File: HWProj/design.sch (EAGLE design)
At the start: 30 parts, among them IC1 LM311N, IC10 TL071P, IC11 TL071P, IC12 TL071P, IC2 TL071P, IC3 TL071P, IC4 TL071P, IC5 LM311N, IC6 TL071P, Q1 2N3904, Q2 2N3904

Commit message: begin designing entire schematic, added power
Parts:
- removed S1: TL32PO, switch:TL32PO
- added C2: 0.0022u, HyTechDevices:CAPCAP_WIMA
- added CN1: (no value), HyTechDevices:DCBARRELPTH
- added DC/DC1: DC/DC-STEP-UP-XL6009, userlib:DC/DC-STEP-UP-XL6009
- added IC13, IC14, IC15, IC17, IC7, IC8, IC9: TL071P, linear:TL071P
- added IC16: LM311N, linear:LM311N
- added Q3, Q4: 2N3904, transistor:2N3904
- added R10: 1.5M, HyTechDevices:RESISTORAXIAL-0.3
- added R12: 1.5k, HyTechDevices:RESISTORAXIAL-0.3
- added R13: 20k, HyTechDevices:RESISTORAXIAL-0.3
- added R14, R17, R18: 12k, HyTechDevices:RESISTORAXIAL-0.3
- added R15, R19, R20, R4: 10k, HyTechDevices:RESISTORAXIAL-0.3
- added R16, R21: 33k, HyTechDevices:RESISTORAXIAL-0.3
- added R9: 5.6k, HyTechDevices:RESISTORAXIAL-0.3
- added TM4: 50k, HyTechDevices:TRIMPOT
- added U$2: PAM8302A_ADAFRUIT, HyTechDevices:PAM8302A_ADAFRUIT
- added U$3: FQP30N06L, HyTechDevices:FQP30N06L
- added U$4: TEENSY_3.5_EXT, HyTechDevices:TEENSY_3.5_EXT
- C3, C4: device HyTechDevices:CAPCAP_WIMA -> HyTechDevices:CAPPTH1
- IC5: value LM311N -> TL071P; device linear:LM311N -> linear:TL071P
- IC6: value TL071P -> LM311N; device linear:TL071P -> linear:LM311N
- R1: value 20k -> 15k
- TM1: value 10K -> 50k
- TM2: value 10k -> 100k
- TM3: value 10k -> 10K
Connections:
- removed net VCO_FREQ_CONTROL: TM3.E
- new net +9V: CN1.PWR, DC/DC1.+VIN, U$4.VIN
- new net 11.5V: IC9.+IN, R4.1, R9.2
- new net COMP_SQ_OUT: IC16.OUT, IC8.+IN, R17.1, R20.2
- new net DGND: CN1.GND, CN1.GNDBREAK, DC/DC1.-VIN, U$4.AGND, U$4.GND
- new net N$13: IC7.OUT, R12.1
- new net N$15: IC6.ON, IC6.ON/STR
- new net N$16: IC15.-IN, IC15.OUT, U$3.G
- new net N$17: IC16.ON, IC16.ON/STR
- new net N$19: IC13.OUT, TM2.E, U$2.A+
- new net N$21: IC7.-IN, Q3.C, R10.1
- new net N$23: IC6.-IN, R18.1, R19.2
- new net N$24: IC1.-IN, R14.1, R15.2
- new net N$26: IC16.-IN, TM3.S
- new net N$28: IC5.-IN, R1.2, TM1.A, TM4.A
- new net N$3: Q3.E, Q4.E, R12.2
- new net SAWTOOTH2: C2.2, IC14.OUT, IC16.+IN, IC6.+IN, U$3.D
- new net SIGNAL1: Q1.B
- new net SIGNAL2: Q3.B
- new net VCC_LM386: IC9.-IN, IC9.OUT, U$2.VIN
- net GND: now also IC13.+IN, IC14.+IN, IC16.GND, IC16.V-, IC17.-IN, IC17.OUT, IC5.+IN, IC6.GND, IC7.+IN, Q4.B, R15.1, R19.1, R20.1, R9.1, U$2.A-, U$2.GND; no longer IC5.GND, TM1.A, TM2.A
- net INPUT2: now also IC5.OUT, R1.1; no longer S1.P
- net LOWPASS_OUT: now also TM2.A
- net N$1: now also IC17.+IN, R16.1, R21.2; no longer IC1.-IN, TM1.S
- net N$11: now also IC8.-IN, IC8.OUT; no longer IC5.ON, IC5.ON/STR
- net N$14: now also C2.1, IC14.-IN, Q4.C, U$3.S; no longer IC6.-IN, IC6.OUT, Q1.B
- net N$4: now also IC13.-IN, TM2.S; no longer IC6.+IN, TM3.S
- net N$8: now also IC15.+IN, IC6.OUT, R13.1; no longer IC5.-IN, TM2.S
- net SAWTOOTH: now also TM1.S; no longer IC5.+IN, S1.O
- net SQUARE: now also IC8.ON2, TM4.S; no longer IC5.OUT, R1.1, S1.S
- net V+: now also DC/DC1.+VOUT, IC13.V+, IC14.V+, IC15.V+, IC16.V+, IC17.V+, IC7.V+, IC8.V+, IC9.V+, R10.2, R13.2, R14.2, R16.2, R17.2, R18.2, R4.2, TM3.E; no longer R1.2, TM1.E, TM2.E
- net V-: now also DC/DC1.-VOUT, IC13.V-, IC14.V-, IC15.V-, IC17.V-, IC7.V-, IC8.V-, IC9.V-, R21.1
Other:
- note added: "+/-15V"
- note added: "add diff amp for signal isolation!!"
- note added: "digital"
- note added: "max 1Vrms input"
- note added: "mixing stage"
- note added: "power"
- note added: "speaker output stage"
- note added: "threshold at 6.8V!"
- note added: "volume control"
- note removed: "signal routing"
- note removed: "solution to create +/- 15V required"
- note removed: "threshold control"
- moved on the sheet: C3, C4, IC10, IC11, IC12, IC5, IC6, R1, R11, R5, R7, R8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

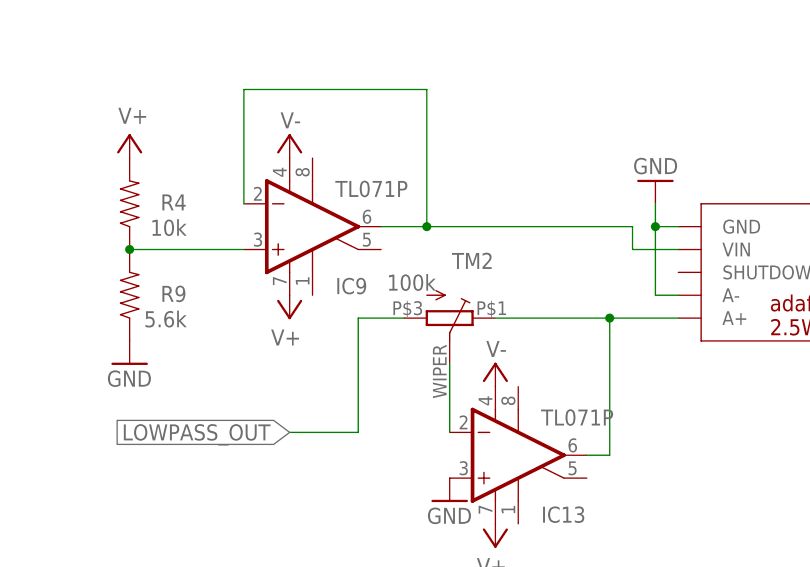
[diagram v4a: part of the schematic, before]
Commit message: changed value of volume control pot at speaker stage to 50k
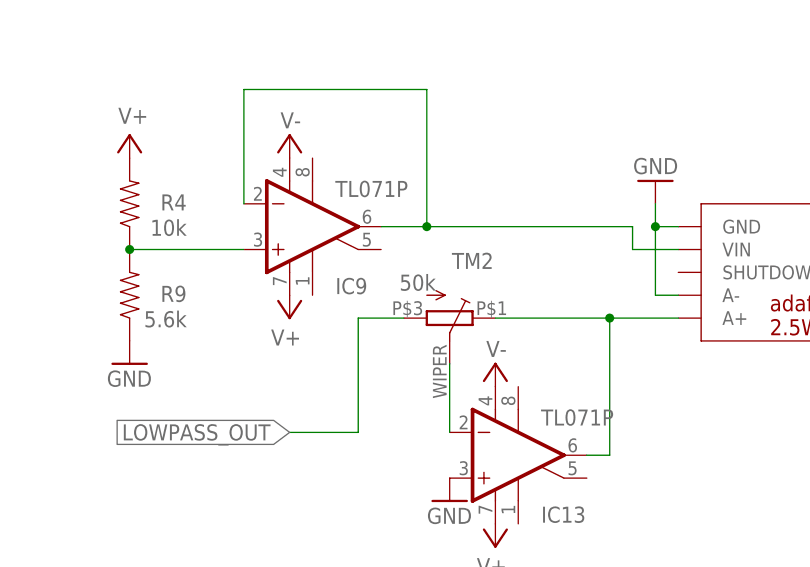
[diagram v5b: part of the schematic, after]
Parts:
- TM2: value 100k -> 50k
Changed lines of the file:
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@@
 <part name="IC13" library="linear" library_urn="urn:adsk.eagle:library:262" deviceset="TL071" device="P" package3d_urn="urn:adsk.eagle:package:16409/2"/>
 <part name="GND18" library="HyTechSymbols" deviceset="GND" device=""/>
-<part name="TM2" library="HyTechDevices" deviceset="TRIMPOT" device="" value="100k"/>
+<part name="TM2" library="HyTechDevices" deviceset="TRIMPOT" device="" value="50k"/>
 <part name="U$2" library="HyTechDevices" deviceset="PAM8302A_ADAFRUIT" device=""/>
 <part name="GND10" library="HyTechSymbols" deviceset="GND" device=""/>

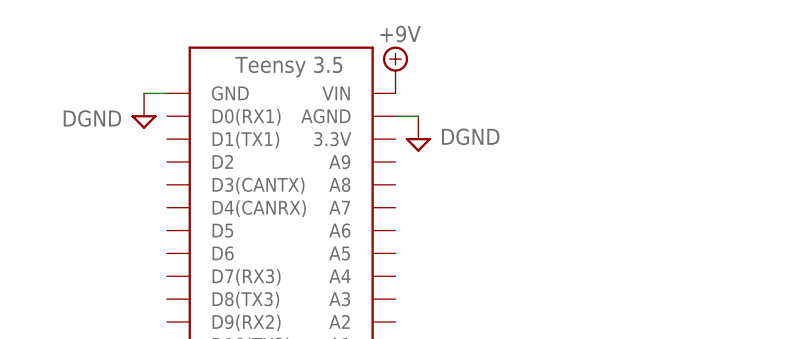
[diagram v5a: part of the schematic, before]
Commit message: corrected teensy vin
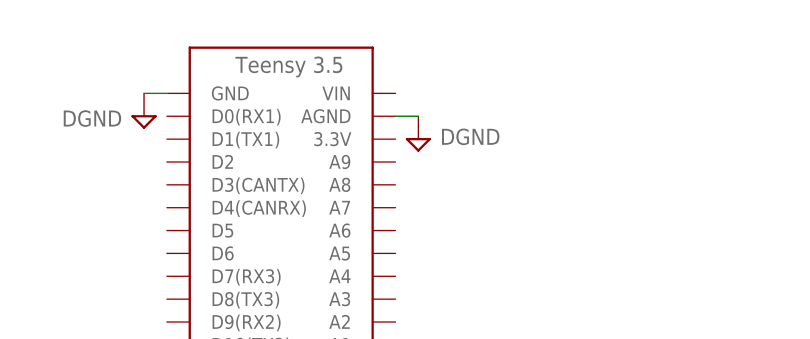
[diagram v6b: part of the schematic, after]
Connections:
- net +9V: no longer U$4.VIN
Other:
- note added: "Vin is in the range of 3.6 - 6.0V !!"
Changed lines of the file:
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@@
 <part name="GND5" library="HyTechSymbols" deviceset="GND" device=""/>
 <part name="U$4" library="HyTechDevices" deviceset="TEENSY_3.5_EXT" device=""/>
-<part name="SUPPLY44" library="supply2" library_urn="urn:adsk.eagle:library:372" deviceset="+9V" device=""/>
 <part name="SUPPLY45" library="supply2" library_urn="urn:adsk.eagle:library:372" deviceset="DGND" device=""/>
 <part name="SUPPLY46" library="supply2" library_urn="urn:adsk.eagle:library:372" deviceset="DGND" device=""/>
@@
 <wire x1="513.08" y1="180.34" x2="144.78" y2="180.34" width="0.254" layer="150"/>
 <text x="325.12" y="274.32" size="2.54" layer="150">digital</text>
+<text x="213.36" y="261.62" size="1.778" layer="150"> Vin is in the range of 3.6 - 6.0V !!</text>
 </plain>
 <instances>
@@
 </instance>
 <instance part="U$4" gate="G$1" x="187.96" y="187.96" smashed="yes"/>
-<instance part="SUPPLY44" gate="G$1" x="210.82" y="259.08" smashed="yes">
-<attribute name="VALUE" x="208.915" y="262.255" size="1.778" layer="96"/>
-</instance>
 <instance part="SUPPLY45" gate="G$1" x="182.88" y="254" smashed="yes">
 <attribute name="VALUE" x="180.467" y="254.635" size="1.778" layer="96" rot="R180"/>
@@
 <junction x="22.86" y="228.6"/>
 </segment>
-<segment>
-<pinref part="U$4" gate="G$1" pin="VIN"/>
-<pinref part="SUPPLY44" gate="G$1" pin="+9V"/>
-</segment>
-</net>
+</net>

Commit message: completed initial design for testing, revisions
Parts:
- added IC18: TL071P, linear:TL071P
- added R22, R25, R26, R28, R29: 200k, HyTechDevices:RESISTORAXIAL-0.3
- added R23, R24, R27: 12k, HyTechDevices:RESISTORAXIAL-0.3
- added SP1: BUZZER, HyTechSymbols:BUZZER
- added TM8: 100k, HyTechDevices:TRIMPOT
- added U$5: DC/DC-STEP-DOWN-XL6009, userlib:DC/DC-STEP-DOWN-XL6009
- R4: value 10k -> 12k
- R9: value 5.6k -> 200k
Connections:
- removed net +9V: CN1.PWR, DC/DC1.+VIN
- removed net 11.5V: IC9.+IN, R4.1, R9.2
- removed net SIGNAL2: Q3.B
- removed net VCC_LM386: IC9.-IN, IC9.OUT, U$2.VIN
- new net +1.8V: IC18.-IN, IC18.OUT, R28.2, R29.2
- new net +5V: U$2.VIN, U$4.VIN, U$5.+VOUT
- new net DAC1: R22.2, U$4.A21
- new net DAC2: R26.2, U$4.A22
- new net DGNDLVL: IC13.-IN, IC13.OUT, R25.2, R9.2
- new net N$27: IC17.-IN, R24.2, R25.1, R29.1
- new net N$30: IC9.-IN, R28.1, R4.2, R9.1
- new net N$31: IC9.+IN, R22.1, R23.1
- new net VCC: CN1.PWR, DC/DC1.+VIN, U$5.+VIN
- net DGND: now also IC13.+IN, U$5.-VIN, U$5.-VOUT
- net GND: now also R16.1, R21.2, R23.2, R27.2, TM2.E, TM8.E, U$2.A+; no longer IC13.+IN, IC17.-IN, IC17.OUT, R9.1, U$2.A-
- net N$1: now also TM2.S, U$2.A-; no longer IC17.+IN, R16.1, R21.2
- net N$11: now also IC17.+IN, R26.1, R27.1; no longer IC8.-IN, IC8.OUT
- net N$19: now also IC17.OUT, Q3.B, R24.1; no longer IC13.OUT, TM2.E, U$2.A+
- net N$4: now also IC18.+IN, TM8.S; no longer IC13.-IN, TM2.S
- net SIGNAL1: now also IC9.OUT, R4.1
- net SQUARE: now also IC8.-IN, IC8.OUT; no longer IC8.ON2
- net V+: now also IC18.V+, TM8.A; no longer R4.2
- net V-: now also IC18.V-
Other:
- note added: "4ohm 5W"
- note added: "hi-z input impedance??"
- note added: "master volume"
- note added: "reference generation"
- note added: "saw volume"
- note added: "square volume"
- note removed: "Vin is in the range of 3.6 - 6.0V !!"
- note removed: "add diff amp for signal isolation!!"
- note removed: "volume control"
- moved on the sheet: C1, C2, C3, C4, CN1, DC/DC1, IC1, IC10, IC11, IC12, IC13, IC14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

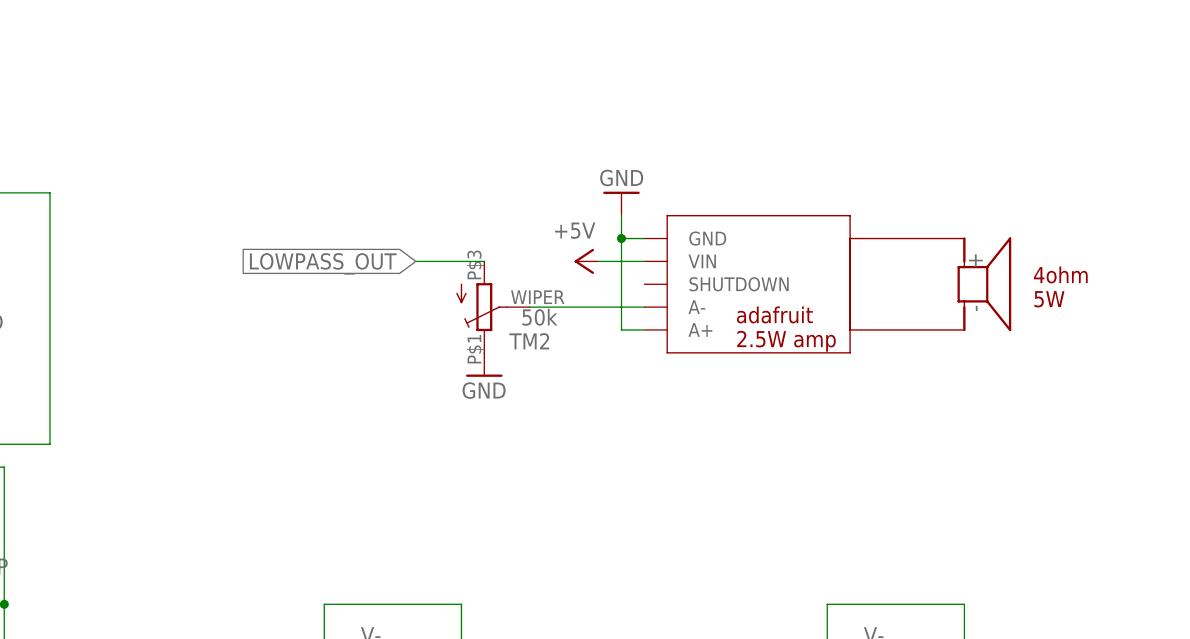
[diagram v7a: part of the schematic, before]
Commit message: added 3.5mm jack
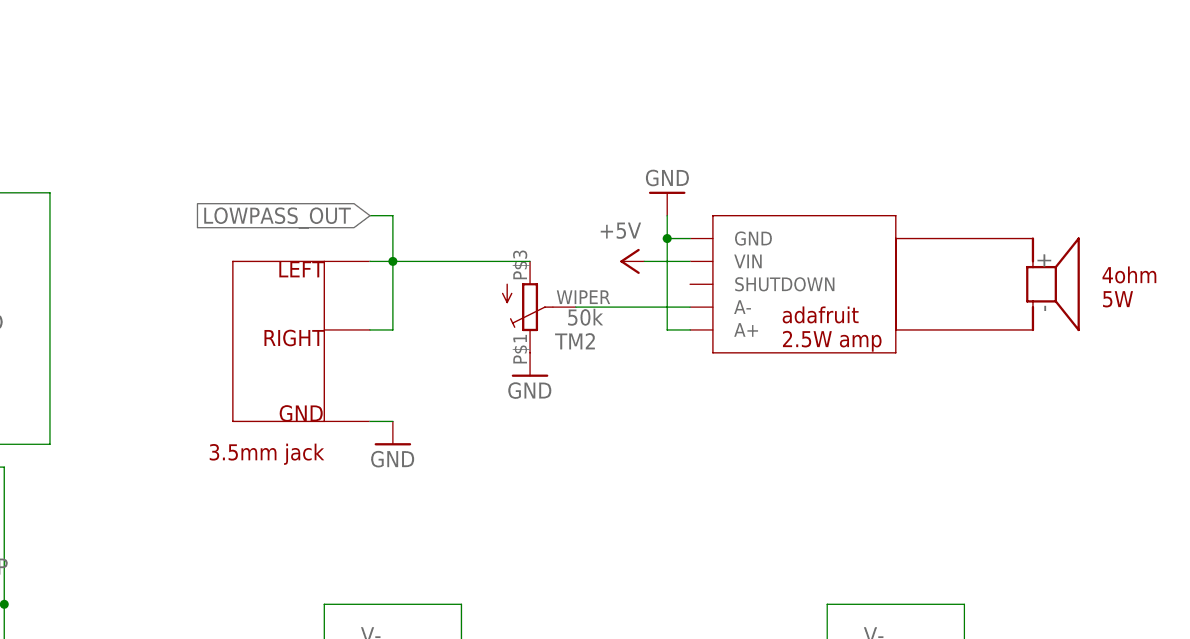
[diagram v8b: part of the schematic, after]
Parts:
- added U$6: 3.5MM_AUDIO_JACK, userlib:3.5MM_AUDIO_JACK
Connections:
- net GND: now also U$6.GND
- net LOWPASS_OUT: now also U$6.L, U$6.R
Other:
- note added: "3.5mm jack"
- note added: "inverted external outputs!!"
- moved on the sheet: TM2
